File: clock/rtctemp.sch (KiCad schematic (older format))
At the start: 13 parts

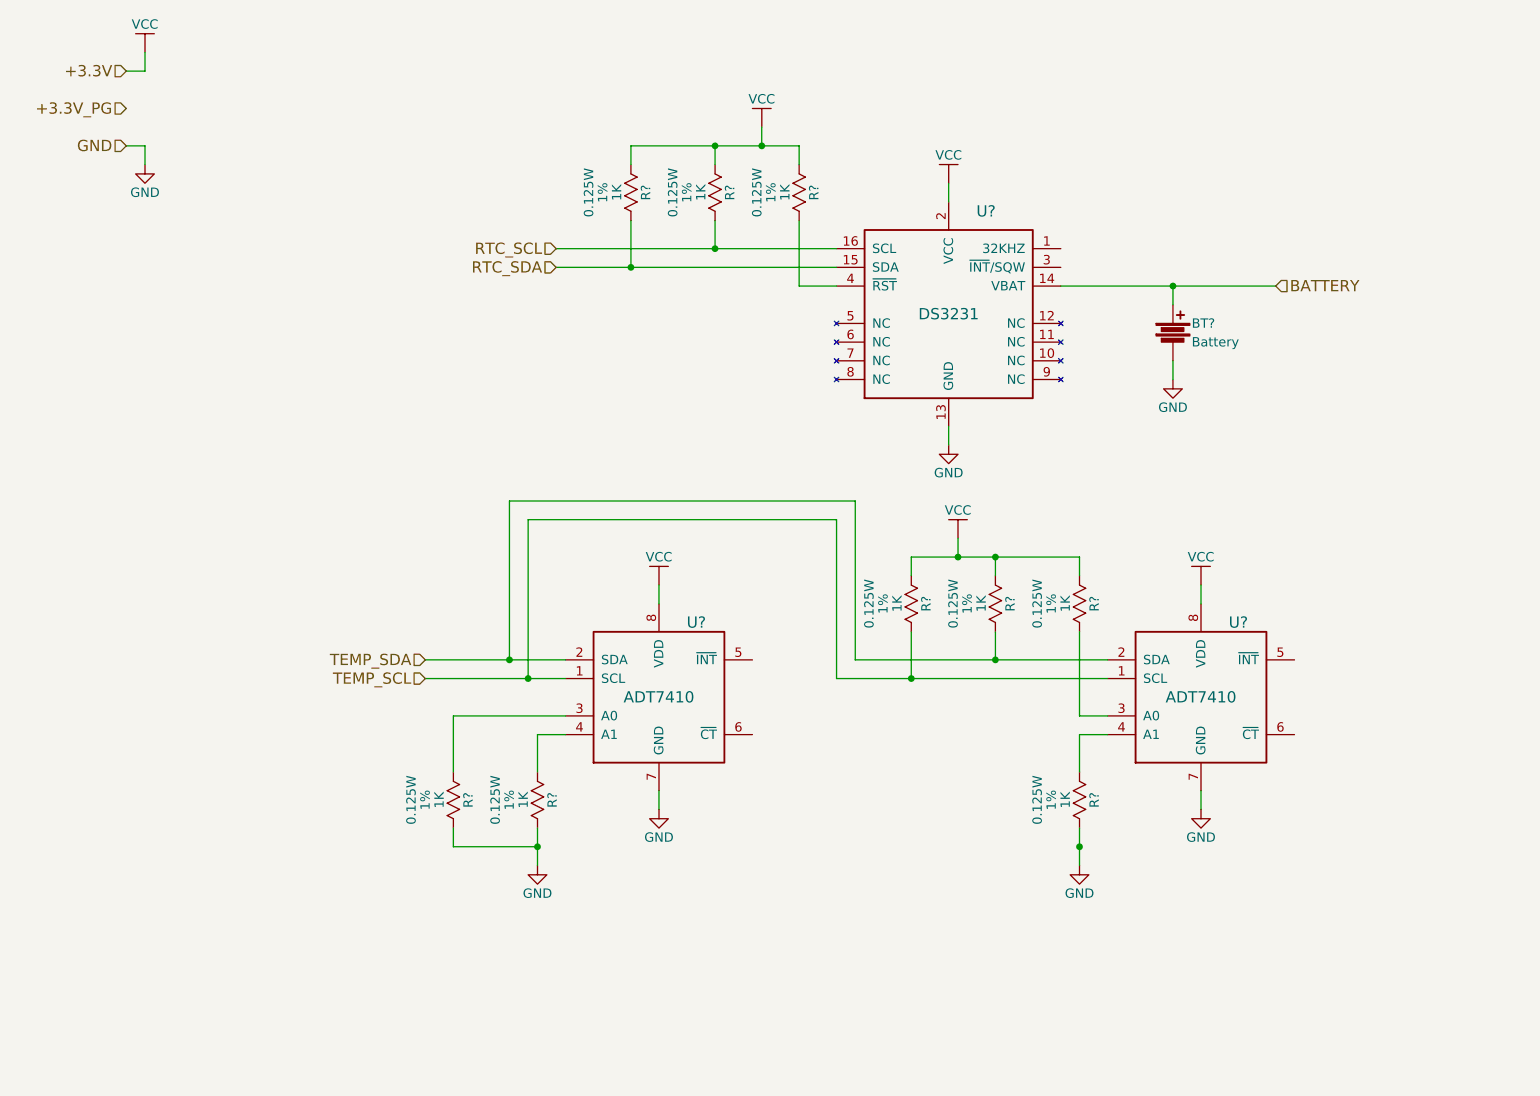
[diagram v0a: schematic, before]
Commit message: Add proper loading and buffer to the OCXO output.
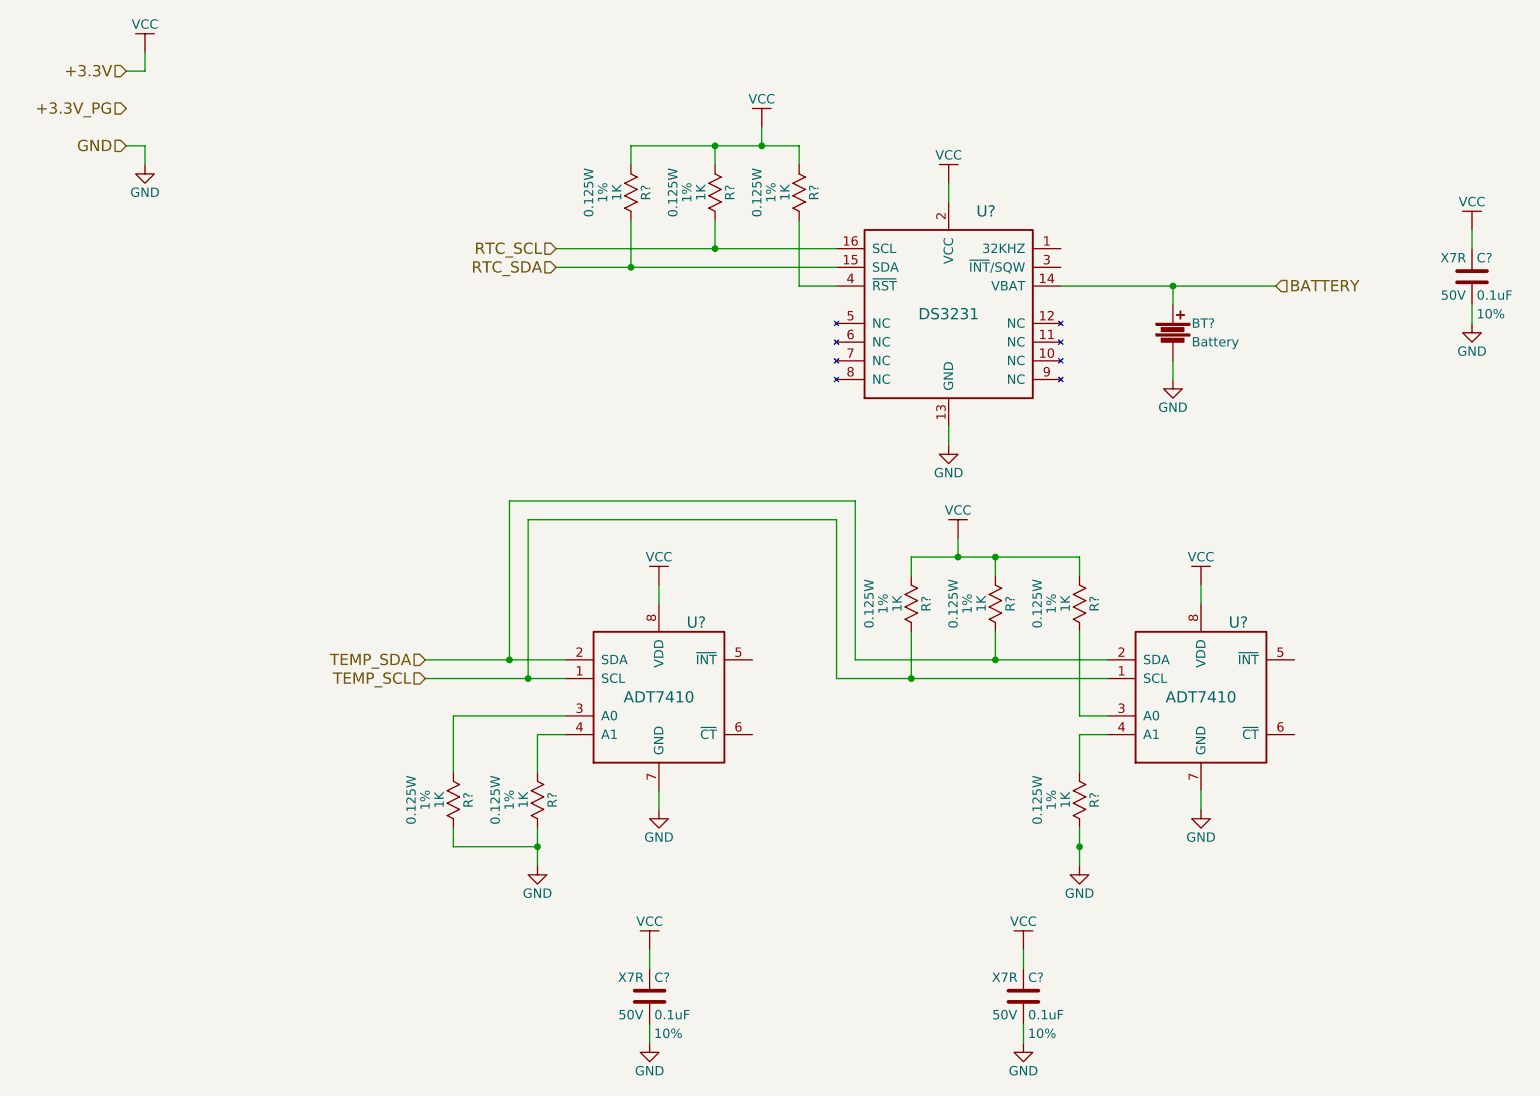
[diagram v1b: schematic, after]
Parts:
- added C? (x3): 0.1uF, Capacitors_SMD:C_0805_HandSoldering, symbol C
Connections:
- net GND: now also C?.2, C?.2, C?.2
- net VCC: now also C?.1, C?.1, C?.1
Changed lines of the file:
@@
 Connection ~ 3400 4550
 Connection ~ 3500 4650
+$Comp
+L GND #PWR?
+U 1 1 5636CF30
+P 8550 2750
+F 0 "#PWR?" H 8550 2500 50  0001 C CNN
+F 1 "GND" H 8550 2600 50  0000 C CNN
+F 2 "" H 8550 2750 60  0000 C CNN
+F 3 "" H 8550 2750 60  0000 C CNN
+	1    8550 2750
+	1    0    0    -1
+$EndComp
+Wire Wire Line
+	8550 2650 8550 2750
+Wire Wire Line
+	8550 2350 8550 2250
+$Comp
+L C C?
+U 1 1 5636CF43
+P 8550 2500
+F 0 "C?" H 8575 2600 50  0000 L CNN
+F 1 "0.1uF" H 8575 2400 50  0000 L CNN
+F 2 "Capacitors_SMD:C_0805_HandSoldering" H 8588 2350 30  0001 C CNN
+F 3 "" H 8550 2500 60  0000 C CNN
+F 4 "50V" H 8450 2400 50  0000 C CNN "Voltage"
+F 5 "10%" H 8650 2300 50  0000 C CNN "Tolerance"
+F 6 "X7R" H 8450 2600 50  0000 C CNN "Dielectric"
+F 7 "Kemet" H 8550 2500 50  0001 C CNN "Manufacturer"
+F 8 "C0805C104K5RACTU" H 8550 2500 50  0001 C CNN "PartNum"
+	1    8550 2500
+	1    0    0    -1
+$EndComp
+$Comp
+L VCC #PWR?
+U 1 1 5636D2DE
+P 8550 2250
+F 0 "#PWR?" H 8550 2100 50  0001 C CNN
+F 1 "VCC" H 8550 2400 50  0000 C CNN
+F 2 "" H 8550 2250 60  0000 C CNN
+F 3 "" H 8550 2250 60  0000 C CNN
+	1    8550 2250
+	1    0    0    -1
+$EndComp
+$Comp
+L GND #PWR?
+U 1 1 5636D43C
+P 4150 6600
+F 0 "#PWR?" H 4150 6350 50  0001 C CNN
+F 1 "GND" H 4150 6450 50  0000 C CNN
+F 2 "" H 4150 6600 60  0000 C CNN
+F 3 "" H 4150 6600 60  0000 C CNN
+	1    4150 6600
+	1    0    0    -1
+$EndComp
+Wire Wire Line
+	4150 6500 4150 6600
+Wire Wire Line
+	4150 6200 4150 6100
+$Comp
+L C C?
+U 1 1 5636D449
+P 4150 6350
+F 0 "C?" H 4175 6450 50  0000 L CNN
+F 1 "0.1uF" H 4175 6250 50  0000 L CNN
+F 2 "Capacitors_SMD:C_0805_HandSoldering" H 4188 6200 30  0001 C CNN
+F 3 "" H 4150 6350 60  0000 C CNN
+F 4 "50V" H 4050 6250 50  0000 C CNN "Voltage"
+F 5 "10%" H 4250 6150 50  0000 C CNN "Tolerance"
+F 6 "X7R" H 4050 6450 50  0000 C CNN "Dielectric"
+F 7 "Kemet" H 4150 6350 50  0001 C CNN "Manufacturer"
+F 8 "C0805C104K5RACTU" H 4150 6350 50  0001 C CNN "PartNum"
+	1    4150 6350
+	1    0    0    -1
+$EndComp
+$Comp
+L VCC #PWR?
+U 1 1 5636D44F
+P 4150 6100
+F 0 "#PWR?" H 4150 5950 50  0001 C CNN
+F 1 "VCC" H 4150 6250 50  0000 C CNN
+F 2 "" H 4150 6100 60  0000 C CNN
+F 3 "" H 4150 6100 60  0000 C CNN
+	1    4150 6100
+	1    0    0    -1
+$EndComp
+$Comp
+L GND #PWR?
+U 1 1 5636D49F
+P 6150 6600
+F 0 "#PWR?" H 6150 6350 50  0001 C CNN
+F 1 "GND" H 6150 6450 50  0000 C CNN
+F 2 "" H 6150 6600 60  0000 C CNN
+F 3 "" H 6150 6600 60  0000 C CNN
+	1    6150 6600
+	1    0    0    -1
+$EndComp
+Wire Wire Line
+	6150 6500 6150 6600
+Wire Wire Line
+	6150 6200 6150 6100
+$Comp
+L C C?
+U 1 1 5636D4AC
+P 6150 6350
+F 0 "C?" H 6175 6450 50  0000 L CNN
+F 1 "0.1uF" H 6175 6250 50  0000 L CNN
+F 2 "Capacitors_SMD:C_0805_HandSoldering" H 6188 6200 30  0001 C CNN
+F 3 "" H 6150 6350 60  0000 C CNN
+F 4 "50V" H 6050 6250 50  0000 C CNN "Voltage"
+F 5 "10%" H 6250 6150 50  0000 C CNN "Tolerance"
+F 6 "X7R" H 6050 6450 50  0000 C CNN "Dielectric"
+F 7 "Kemet" H 6150 6350 50  0001 C CNN "Manufacturer"
+F 8 "C0805C104K5RACTU" H 6150 6350 50  0001 C CNN "PartNum"
+	1    6150 6350
+	1    0    0    -1
+$EndComp
+$Comp
+L VCC #PWR?
+U 1 1 5636D4B2
+P 6150 6100
+F 0 "#PWR?" H 6150 5950 50  0001 C CNN
+F 1 "VCC" H 6150 6250 50  0000 C CNN
+F 2 "" H 6150 6100 60  0000 C CNN
+F 3 "" H 6150 6100 60  0000 C CNN
+	1    6150 6100
+	1    0    0    -1
+$EndComp
 $EndSCHEMATC

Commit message: Fan and power connectors.
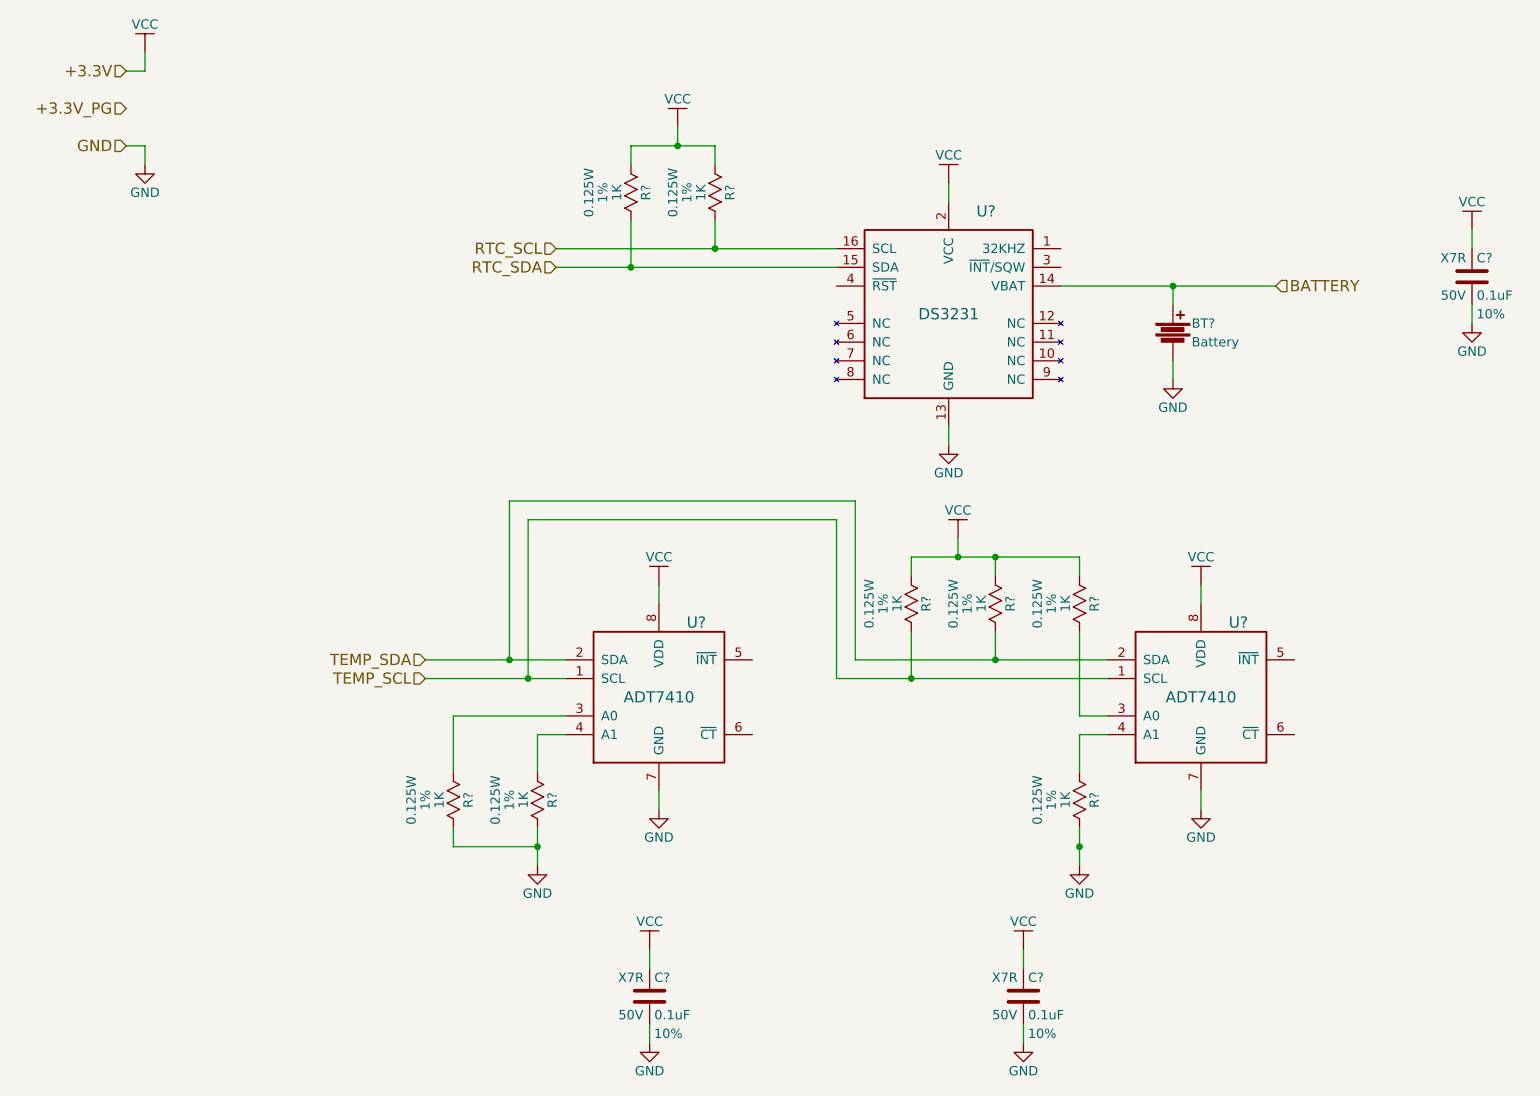
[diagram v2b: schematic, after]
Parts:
- removed R?: 1K, Resistors_SMD:R_0805_HandSoldering, symbol R_local
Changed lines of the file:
@@
 $EndComp
 Wire Wire Line
-	3650 2350 5150 2350
+	3650 2350 4500 2350
+Wire Wire Line
+	4500 2350 5150 2350
 Wire Wire Line
 	4500 2350 4500 2200
 Wire Wire Line
-	3650 2450 5150 2450
+	3650 2450 4050 2450
+Wire Wire Line
+	4050 2450 5150 2450
 Wire Wire Line
 	4050 2450 4050 2200
@@
 	4050 1900 4050 1800
 Wire Wire Line
-	4750 1800 4750 1700
+	4300 1800 4300 1700
 Wire Wire Line
 	4500 1800 4500 1900
@@
 L VCC #PWR?
 U 1 1 5636BBAE
-P 4750 1700
-F 0 "#PWR?" H 4750 1550 50  0001 C CNN
-F 1 "VCC" H 4750 1850 50  0000 C CNN
-F 2 "" H 4750 1700 60  0000 C CNN
-F 3 "" H 4750 1700 60  0000 C CNN
-	1    4750 1700
+P 4300 1700
+F 0 "#PWR?" H 4300 1550 50  0001 C CNN
+F 1 "VCC" H 4300 1850 50  0000 C CNN
+F 2 "" H 4300 1700 60  0000 C CNN
+F 3 "" H 4300 1700 60  0000 C CNN
+	1    4300 1700
 	1    0    0    -1
 $EndComp
@@
 $EndComp
 Wire Wire Line
-	6350 2550 7500 2550
+	6350 2550 6950 2550
+Wire Wire Line
+	6950 2550 7500 2550
 Wire Wire Line
 	6950 2550 6950 2650
@@
 BATTERY
 Connection ~ 6950 2550
-$Comp
-L R_local R?
-U 1 1 5636BE04
-P 4950 2050
-F 0 "R?" V 5030 2050 50  0000 C CNN
-F 1 "1K" V 4875 2050 50  0000 C CNN
-F 2 "Resistors_SMD:R_0805_HandSoldering" V 4880 2050 30  0001 C CNN
-F 3 "" V 5030 2050 30  0000 C CNN
-F 4 "1%" V 4800 2050 50  0000 C CNN "Tolerance"
-F 5 "0.125W" V 4725 2050 50  0000 C CNN "Power"
-F 6 "Vishay Dale" V 4950 2050 50  0001 C CNN "Manufacturer"
-F 7 "CRCW08051K00FKEA" V 5100 2050 50  0001 C CNN "PartNum"
-	1    4950 2050
-	1    0    0    -1
-$EndComp
-Wire Wire Line
-	4950 2200 4950 2550
-Wire Wire Line
-	4950 2550 5150 2550
-Wire Wire Line
-	4950 1800 4950 1900
-Connection ~ 4500 1800
-Connection ~ 4750 1800
-Wire Wire Line
-	4050 1800 4950 1800
+Connection ~ 4300 1800
+Wire Wire Line
+	4050 1800 4500 1800
 Connection ~ 4500 2350
 $Comp
@@
 $EndComp
 Wire Wire Line
-	5550 4000 6450 4000
+	5550 4000 5800 4000
+Wire Wire Line
+	5800 4000 6000 4000
+Wire Wire Line
+	6000 4000 6450 4000
 Connection ~ 5800 4000
 Wire Wire Line
-	5250 4550 6600 4550
+	5250 4550 6000 4550
+Wire Wire Line
+	6000 4550 6600 4550
 Wire Wire Line
 	5250 4550 5250 3700
@@
 	3400 3700 3400 4550
 Wire Wire Line
-	2950 4550 3700 4550
+	2950 4550 3400 4550
+Wire Wire Line
+	3400 4550 3700 4550
 Connection ~ 6000 4550
 Wire Wire Line
-	5150 4650 6600 4650
+	5150 4650 5550 4650
+Wire Wire Line
+	5550 4650 6600 4650
 Wire Wire Line
 	5150 4650 5150 3800
@@
 	3500 3800 3500 4650
 Wire Wire Line
-	2950 4650 3700 4650
+	2950 4650 3500 4650
+Wire Wire Line
+	3500 4650 3700 4650
 Connection ~ 5550 4650
 $Comp
@@
 	3100 4850 3100 5150
 Wire Wire Line
-	3550 5450 3550 5650
+	3550 5450 3550 5550
+Wire Wire Line
+	3550 5550 3550 5650
 Wire Wire Line
 	3550 5550 3100 5550
@@
 	6450 4950 6450 5150
 Wire Wire Line
-	6450 5450 6450 5650
+	6450 5450 6450 5550
+Wire Wire Line
+	6450 5550 6450 5650
 Connection ~ 6450 5550
 $Comp

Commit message: Correct footprint selection. Start pcb. Add BOM files.
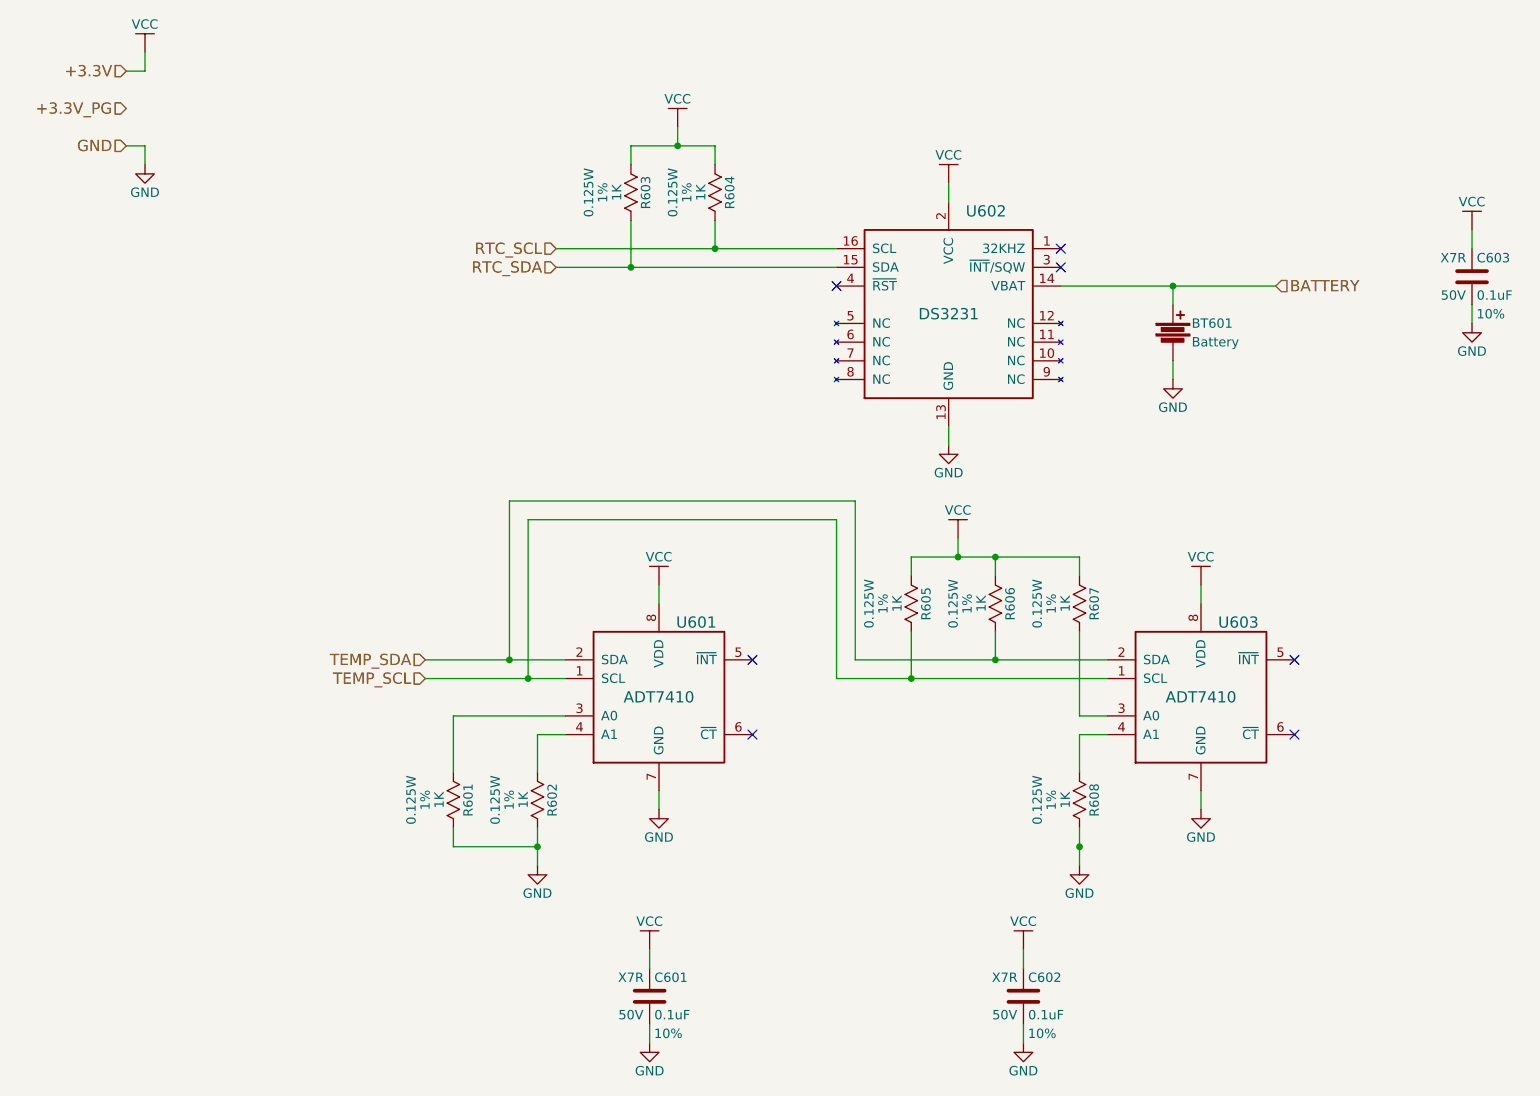
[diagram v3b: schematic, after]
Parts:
- U601, U603: renamed from U?; footprint (none) -> Housings_SOIC:SOIC-8_3.9x4.9mm_Pitch1.27mm
- U602: renamed from U?; footprint (none) -> local:SOIC-16_Maxim_W16_H2
- gave numbers to parts that had none: 12
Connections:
- no-connect marks 0 -> 7
